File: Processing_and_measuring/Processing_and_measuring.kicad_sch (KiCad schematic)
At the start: 37 parts, among them J1 Conn_02x07_Counter_Clockwise, J2 Conn_01x02_Pin, J3 Conn_02x07_Counter_Clockwise, U1 TPL7407LAD, U2 CD74HC4067M, U3 AVR128DA48x-xPT, U4 TPL7407LAD, Y1 X_Crystal_16MHz_18pF

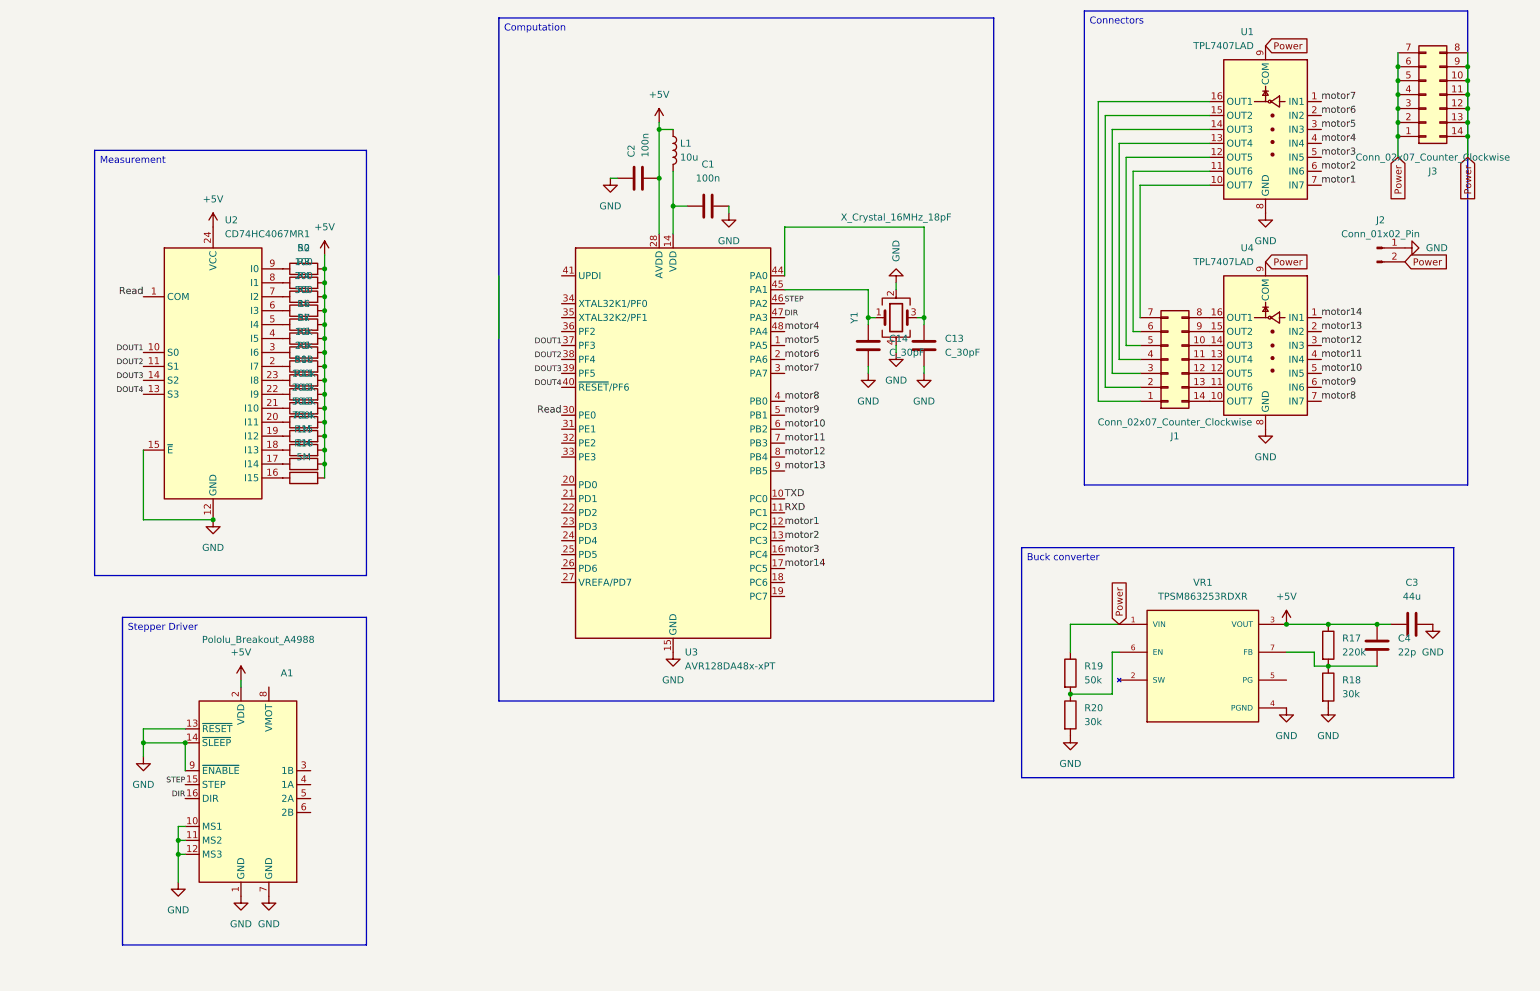
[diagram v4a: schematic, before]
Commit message: Connector for motor
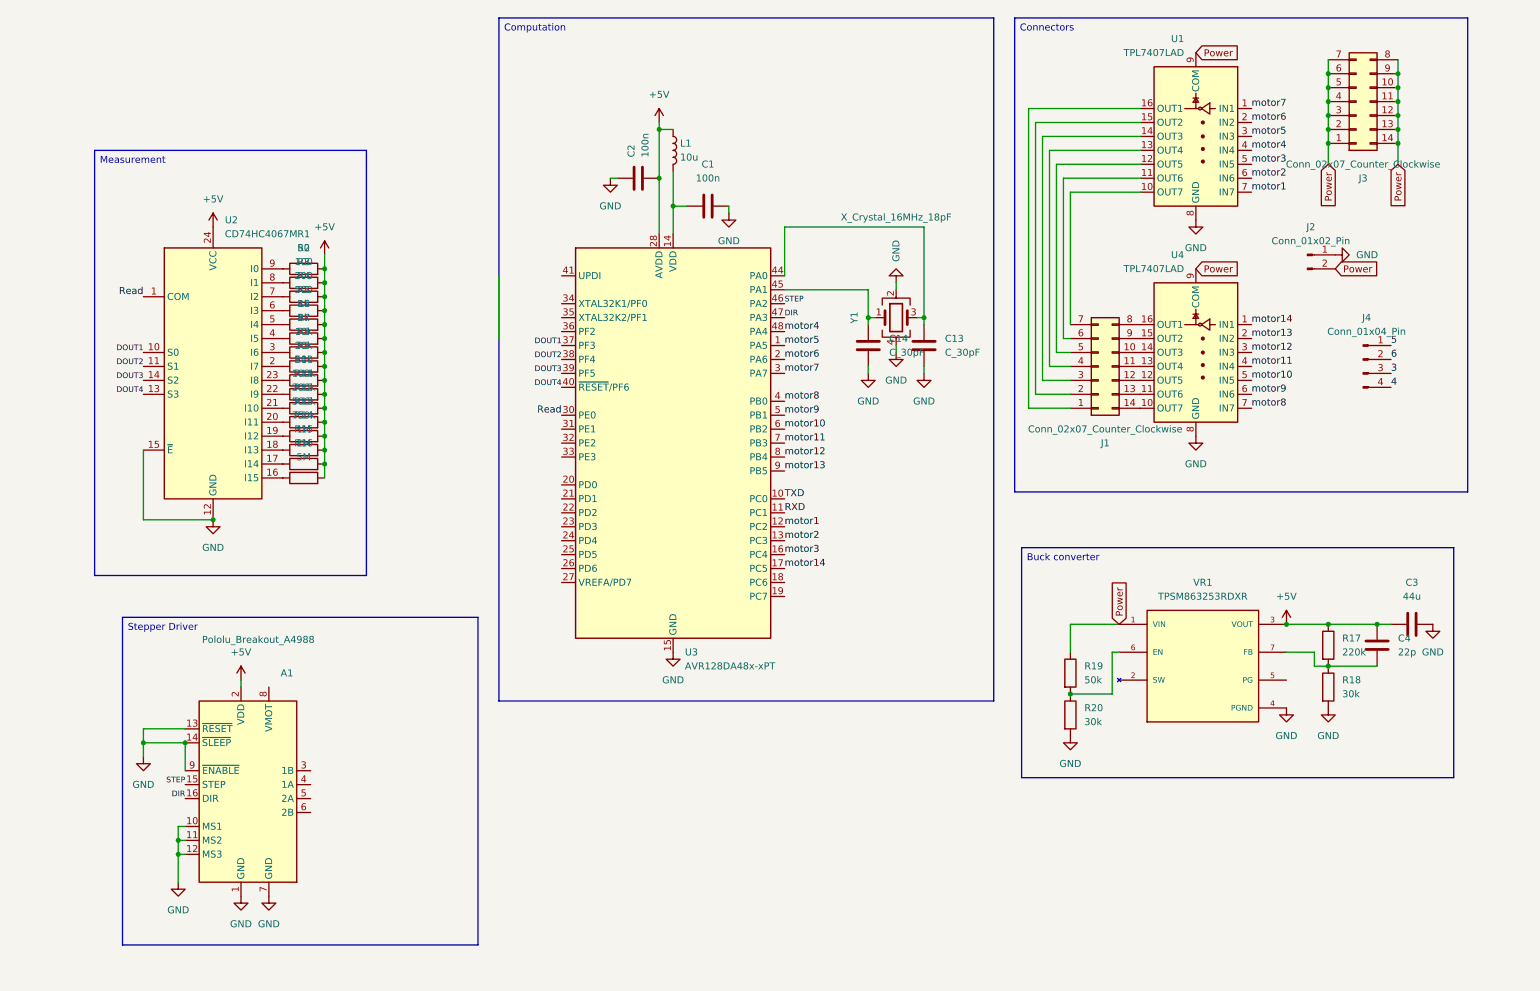
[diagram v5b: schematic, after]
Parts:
- added J4: Conn_01x04_Pin, symbol Connector:Conn_01x04_Pin
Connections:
- new net 3: J4.3 (Pin_3)
- new net 4: J4.4 (Pin_4)
- new net 5: J4.1 (Pin_1)
- new net 6: J4.2 (Pin_2)
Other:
- moved on the sheet: J1, J2, J3, U1, U4

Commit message: More combining
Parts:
- removed J1: Conn_02x07_Counter_Clockwise, Connector_PinHeader_1.00mm:PinHeader_2x07_P1.00mm_Horizontal, symbol Connector_Generic:Conn_02x07_Counter_Clockwise
- added J5: Conn_02x07_Counter_Clockwise, Connector_PinHeader_1.00mm:PinHeader_2x07_P1.00mm_Horizontal, symbol Connector_Generic:Conn_02x07_Counter_Clockwise
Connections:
- net Power: now also A1.8 (VMOT)
- net at U1.16 (OUT1): now also J5.6 (Pin_6)
- net at U4.14 (OUT3): now also J5.13 (Pin_13)
- net at U4.13 (OUT4): now also J5.14 (Pin_14)
- net at U4.12 (OUT5): now also J5.12 (Pin_12)
- net at U4.11 (OUT6): now also J5.10 (Pin_10)
- net at U4.10 (OUT7): now also J5.8 (Pin_8)
- net at U1.15 (OUT2): now also J5.4 (Pin_4)
- net at U1.14 (OUT3): now also J5.2 (Pin_2)
- net at U1.13 (OUT4): now also J5.1 (Pin_1)
- net at U1.12 (OUT5): now also J5.3 (Pin_3)
- net at U1.11 (OUT6): now also J5.5 (Pin_5)
- net at U1.10 (OUT7): now also J5.7 (Pin_7)
- net at U4.16 (OUT1): now also J5.9 (Pin_9)
- net at U4.15 (OUT2): now also J5.11 (Pin_11)

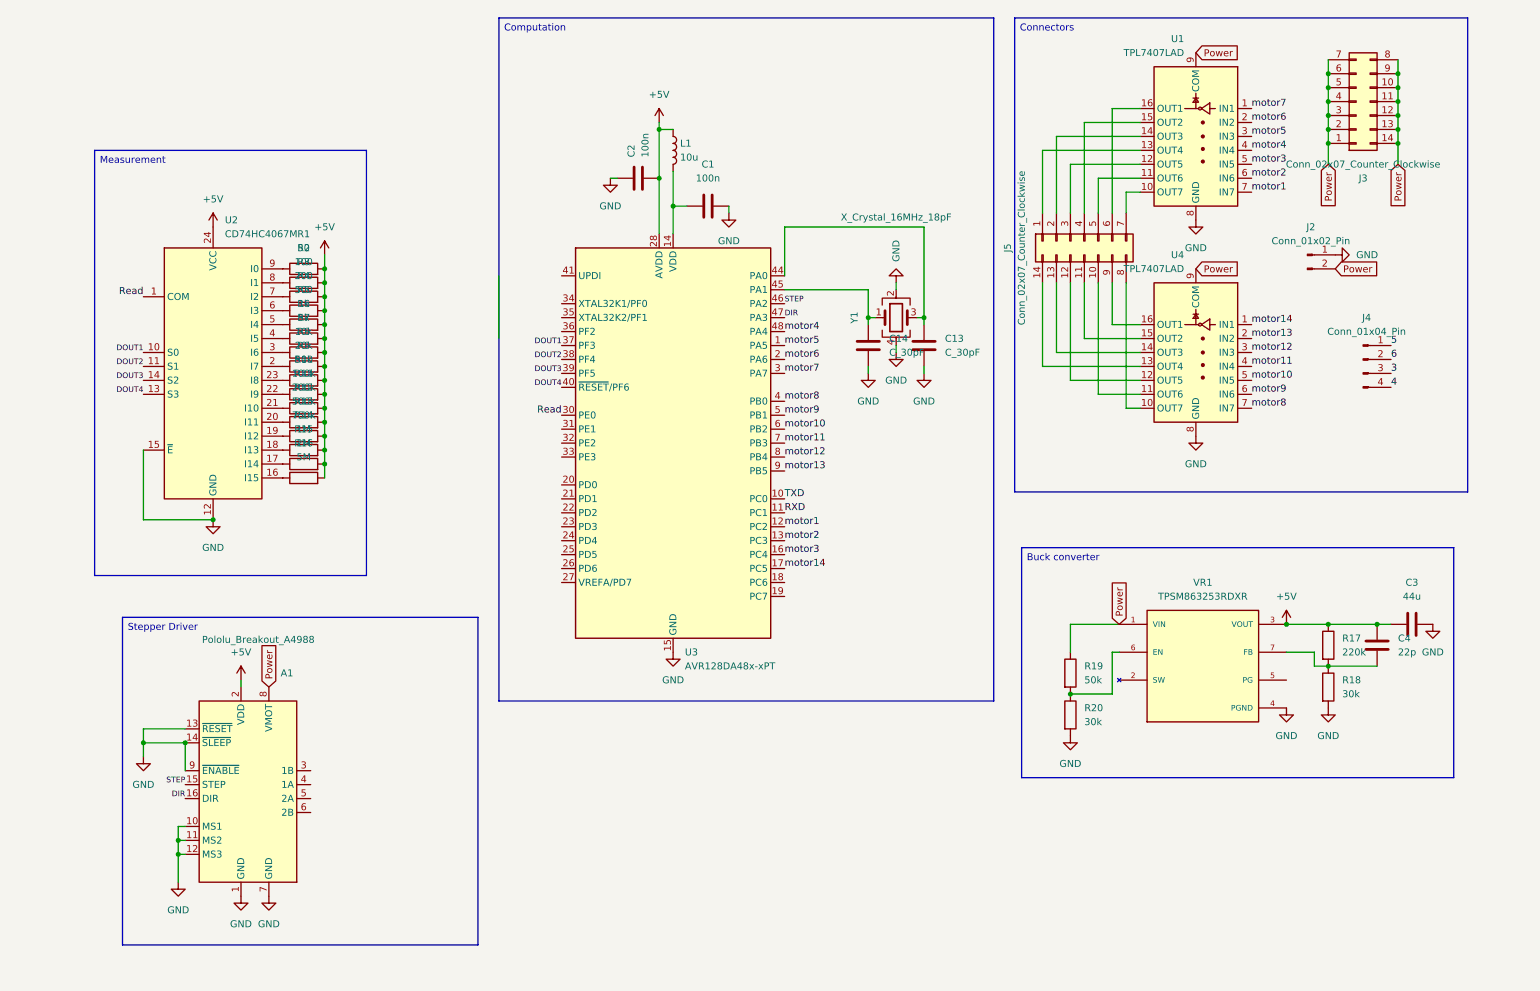
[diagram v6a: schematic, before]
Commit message: Corrected resistor footprints
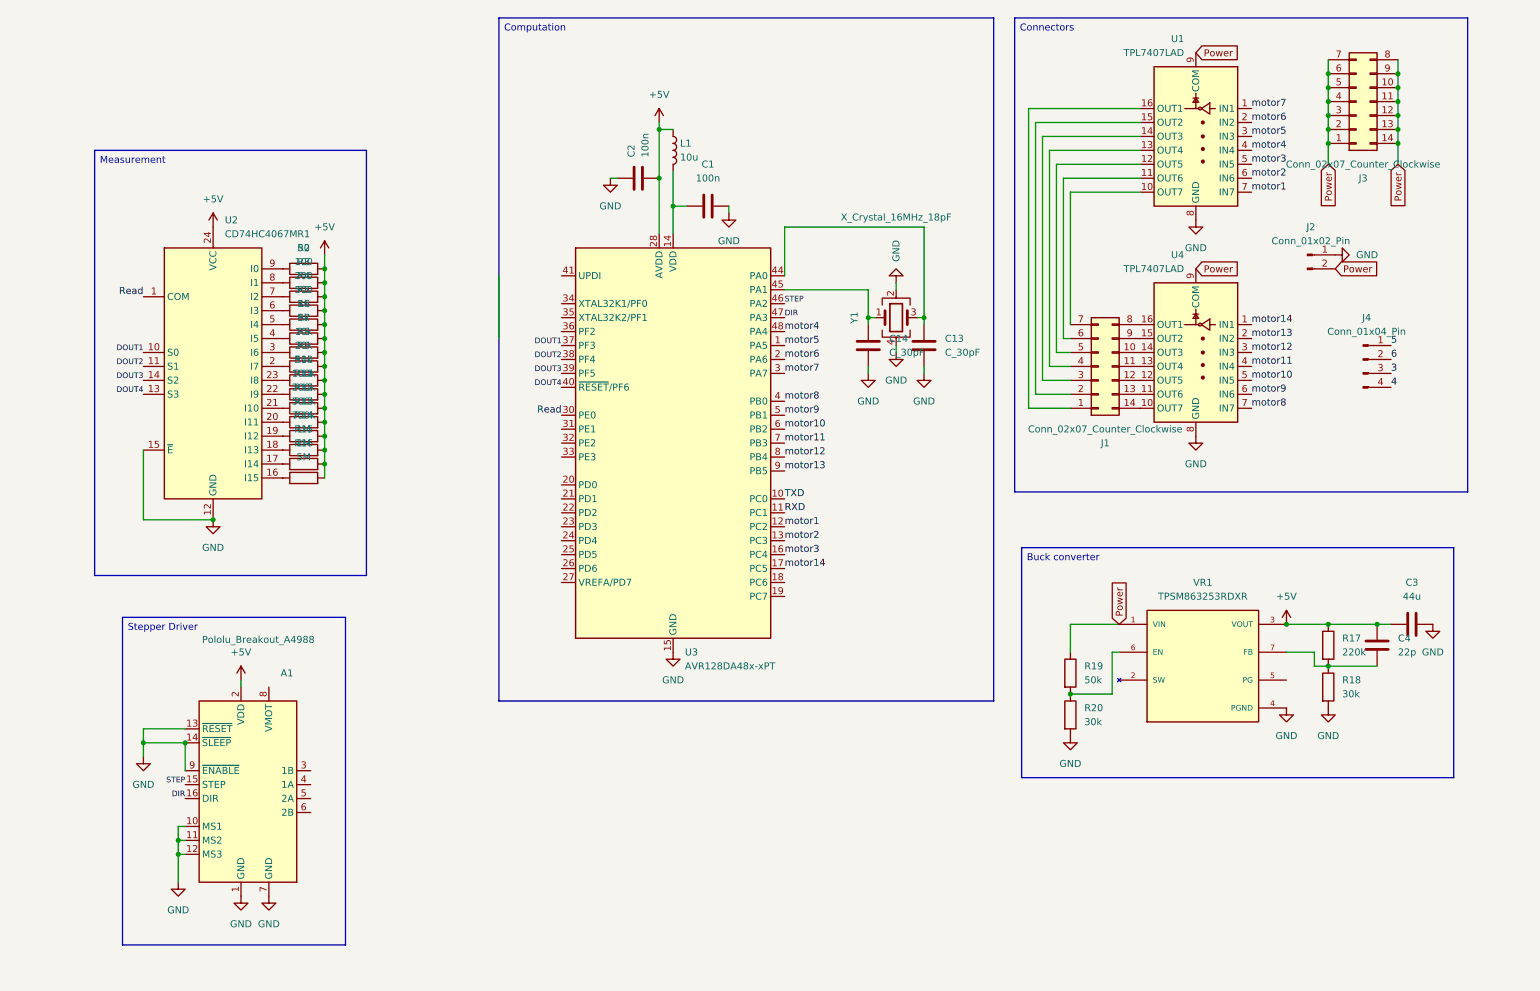
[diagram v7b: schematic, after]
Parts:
- removed J5: Conn_02x07_Counter_Clockwise, Connector_PinHeader_1.00mm:PinHeader_2x07_P1.00mm_Horizontal, symbol Connector_Generic:Conn_02x07_Counter_Clockwise
- added J1: Conn_02x07_Counter_Clockwise, Connector_PinHeader_1.00mm:PinHeader_2x07_P1.00mm_Horizontal, symbol Connector_Generic:Conn_02x07_Counter_Clockwise
- J4: footprint (none) -> Connector_PinHeader_1.00mm:PinHeader_1x04_P1.00mm_Horizontal
- L1: footprint Capacitor_SMD:C_0603_1608Metric -> Inductor_SMD:L_0603_1608Metric
- R1, R10, R11, R12, R13, R14, R15, R16, R17, R18, R19, R2, R20, R3, R4, R5, R6, R7, R8, R9: footprint Capacitor_SMD:C_0603_1608Metric -> Resistor_SMD:R_0603_1608Metric
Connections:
- net Power: no longer A1.8 (VMOT)
- net at U4.10 (OUT7): now also J1.14 (Pin_14)
- net at U4.11 (OUT6): now also J1.13 (Pin_13)
- net at U4.12 (OUT5): now also J1.12 (Pin_12)
- net at U4.13 (OUT4): now also J1.11 (Pin_11)
- net at U4.14 (OUT3): now also J1.10 (Pin_10)
- net at U4.15 (OUT2): now also J1.9 (Pin_9)
- net at U4.16 (OUT1): now also J1.8 (Pin_8)
- net at U1.10 (OUT7): now also J1.7 (Pin_7)
- net at U1.11 (OUT6): now also J1.6 (Pin_6)
- net at U1.12 (OUT5): now also J1.5 (Pin_5)
- net at U1.13 (OUT4): now also J1.4 (Pin_4)
- net at U1.14 (OUT3): now also J1.3 (Pin_3)
- net at U1.15 (OUT2): now also J1.2 (Pin_2)
- net at U1.16 (OUT1): now also J1.1 (Pin_1)

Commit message: more changes to layout
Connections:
- net at J1.1 (Pin_1): now also U1.13 (OUT4); no longer U1.16 (OUT1)
- net at J1.10 (Pin_10): now also U4.11 (OUT6); no longer U4.14 (OUT3)
- net at J1.11 (Pin_11): now also U4.15 (OUT2); no longer U4.13 (OUT4)
- net at J1.13 (Pin_13): now also U4.14 (OUT3); no longer U4.11 (OUT6)
- net at J1.14 (Pin_14): now also U4.13 (OUT4); no longer U4.10 (OUT7)
- net at J1.2 (Pin_2): now also U1.14 (OUT3); no longer U1.15 (OUT2)
- net at J1.3 (Pin_3): now also U1.12 (OUT5); no longer U1.14 (OUT3)
- net at J1.4 (Pin_4): now also U1.15 (OUT2); no longer U1.13 (OUT4)
- net at J1.5 (Pin_5): now also U1.11 (OUT6); no longer U1.12 (OUT5)
- net at J1.6 (Pin_6): now also U1.16 (OUT1); no longer U1.11 (OUT6)
- net at J1.8 (Pin_8): now also U4.10 (OUT7); no longer U4.16 (OUT1)
- net at J1.9 (Pin_9): now also U4.16 (OUT1); no longer U4.15 (OUT2)
- no-connect marks 0 -> 13
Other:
- moved on the sheet: J1
